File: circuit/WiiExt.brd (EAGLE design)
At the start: 63.2 x 30.5 mm, 7 parts

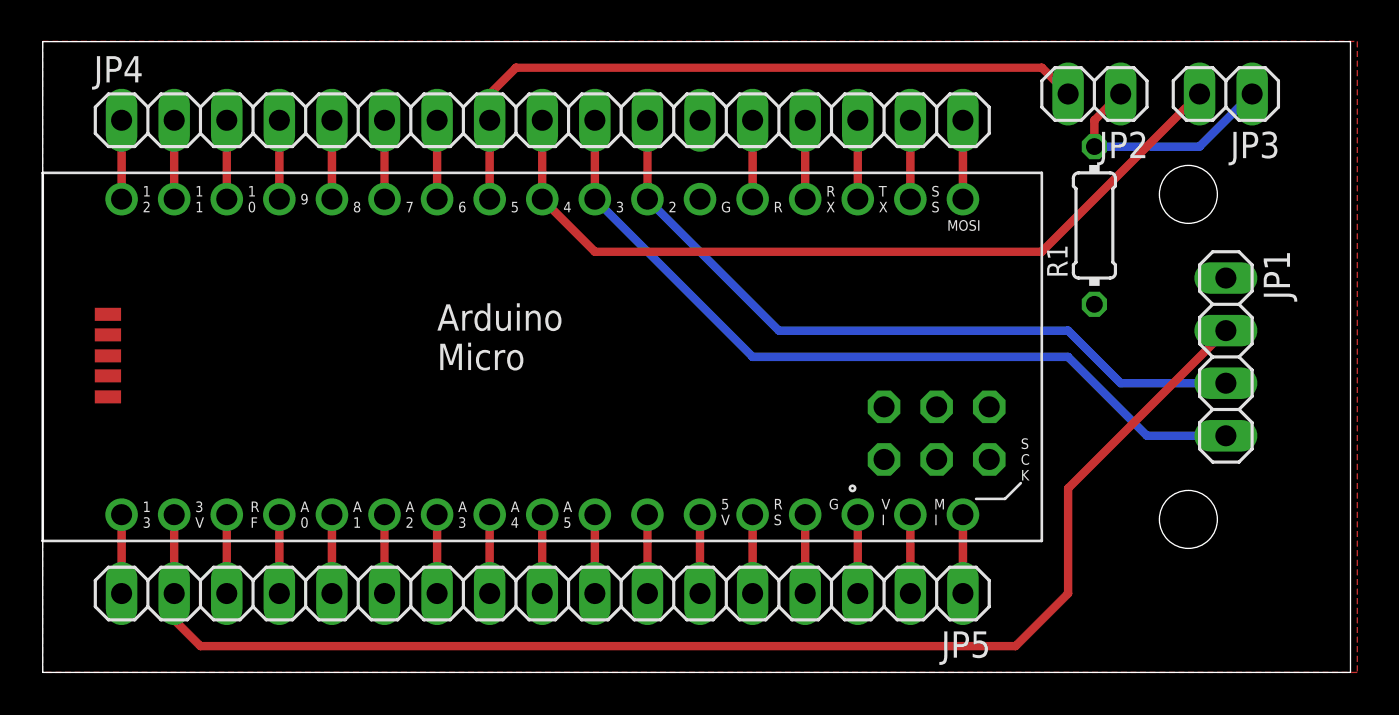
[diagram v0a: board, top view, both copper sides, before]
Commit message: Updated with guitar hero guitar parsing. Added guitar hero guitar example.
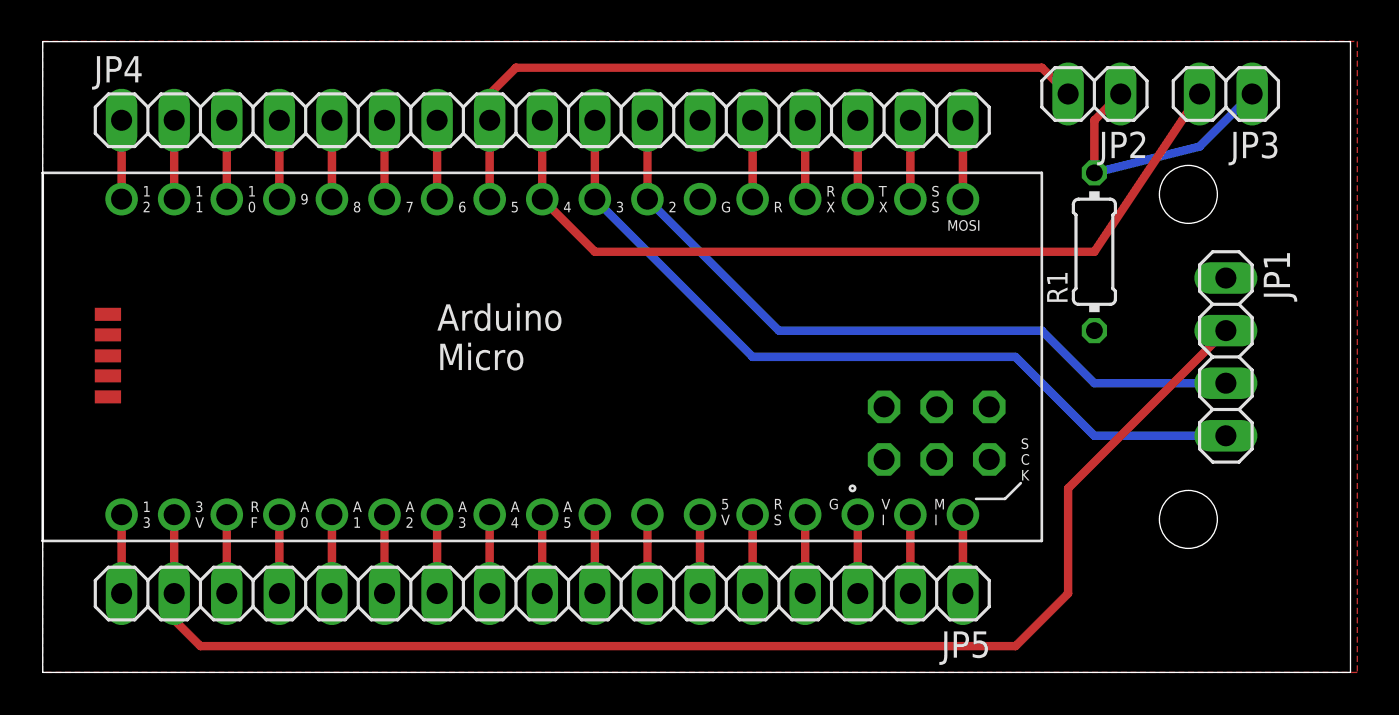
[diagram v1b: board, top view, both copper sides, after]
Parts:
- moved R1 1.27 mm to (50.8, 20.3)
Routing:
- net N$35: track 11.7 -> 13.2 mm
- net N$13: track 39.8 -> 40.7 mm
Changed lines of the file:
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@@
 <element name="JP4" library="pinhead" package="1X17" value="" x="24.13" y="26.67"/>
 <element name="JP5" library="pinhead" package="1X17" value="" x="24.13" y="3.81" rot="R180"/>
-<element name="R1" library="resistor" package="0204/7" value="10k" x="50.8" y="21.59" rot="R90"/>
+<element name="R1" library="resistor" package="0204/7" value="10k" x="50.8" y="20.32" rot="R90"/>
 </elements>
 <signals>
@@
 <wire x1="26.67" y1="26.67" x2="26.67" y2="22.86" width="0.4064" layer="1"/>
 <wire x1="26.67" y1="22.86" x2="34.29" y2="15.24" width="0.4064" layer="16"/>
-<wire x1="34.29" y1="15.24" x2="49.53" y2="15.24" width="0.4064" layer="16"/>
-<wire x1="49.53" y1="15.24" x2="53.34" y2="11.43" width="0.4064" layer="16"/>
-<wire x1="53.34" y1="11.43" x2="57.15" y2="11.43" width="0.4064" layer="16"/>
+<wire x1="34.29" y1="15.24" x2="46.99" y2="15.24" width="0.4064" layer="16"/>
+<wire x1="46.99" y1="15.24" x2="50.8" y2="11.43" width="0.4064" layer="16"/>
+<wire x1="50.8" y1="11.43" x2="57.15" y2="11.43" width="0.4064" layer="16"/>
 </signal>
 <signal name="N$2">
@@
 <wire x1="29.21" y1="26.67" x2="29.21" y2="22.86" width="0.4064" layer="1"/>
 <wire x1="29.21" y1="22.86" x2="35.56" y2="16.51" width="0.4064" layer="16"/>
-<wire x1="35.56" y1="16.51" x2="49.53" y2="16.51" width="0.4064" layer="16"/>
-<wire x1="49.53" y1="16.51" x2="52.07" y2="13.97" width="0.4064" layer="16"/>
-<wire x1="52.07" y1="13.97" x2="57.15" y2="13.97" width="0.4064" layer="16"/>
+<wire x1="35.56" y1="16.51" x2="48.26" y2="16.51" width="0.4064" layer="16"/>
+<wire x1="48.26" y1="16.51" x2="50.8" y2="13.97" width="0.4064" layer="16"/>
+<wire x1="50.8" y1="13.97" x2="57.15" y2="13.97" width="0.4064" layer="16"/>
 </signal>
 <signal name="N$4">
@@
 <wire x1="24.13" y1="26.67" x2="24.13" y2="22.86" width="0.4064" layer="1"/>
 <contactref element="JP3" pad="2"/>
-<wire x1="55.88" y1="27.94" x2="48.26" y2="20.32" width="0.4064" layer="1"/>
-<wire x1="48.26" y1="20.32" x2="26.67" y2="20.32" width="0.4064" layer="1"/>
+<wire x1="55.88" y1="27.94" x2="50.8" y2="20.32" width="0.4064" layer="1"/>
+<wire x1="50.8" y1="20.32" x2="26.67" y2="20.32" width="0.4064" layer="1"/>
 <wire x1="26.67" y1="20.32" x2="24.13" y2="22.86" width="0.4064" layer="1"/>
 </signal>
@@
 <contactref element="JP2" pad="1"/>
 <wire x1="52.07" y1="27.94" x2="50.8" y2="26.67" width="0.4064" layer="1"/>
-<wire x1="50.8" y1="26.67" x2="50.8" y2="25.4" width="0.4064" layer="1"/>
+<wire x1="50.8" y1="26.67" x2="50.8" y2="24.13" width="0.4064" layer="1"/>
 <wire x1="58.42" y1="27.94" x2="55.88" y2="25.4" width="0.4064" layer="16"/>
-<wire x1="55.88" y1="25.4" x2="50.8" y2="25.4" width="0.4064" layer="16"/>
+<wire x1="55.88" y1="25.4" x2="50.8" y2="24.13" width="0.4064" layer="16"/>
 </signal>
 </signals>
